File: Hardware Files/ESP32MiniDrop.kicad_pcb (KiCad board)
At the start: 2 copper layers, 74 x 54 mm, 52 parts, among them J1 USB_B_Mini, J2 Barrel_Jack, J3 AudioJack3, J4 Solenoid1 Terminal, J5 0.100" 2x4 Header, Q1 S8050, Q2 S8050, Q3 NMOS 60V 46A, SW1 SPST (RED), SW2 SPST (BLUE)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

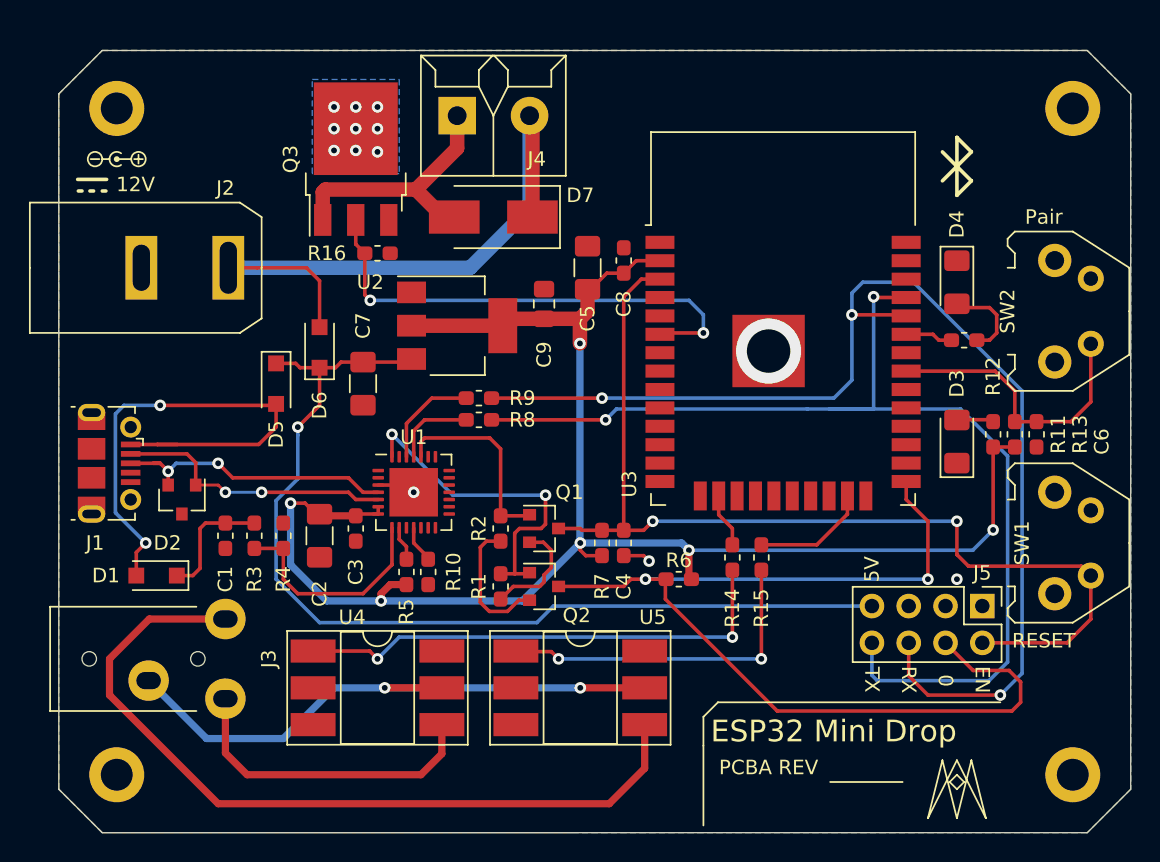
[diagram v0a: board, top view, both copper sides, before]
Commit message: Update project footprint library
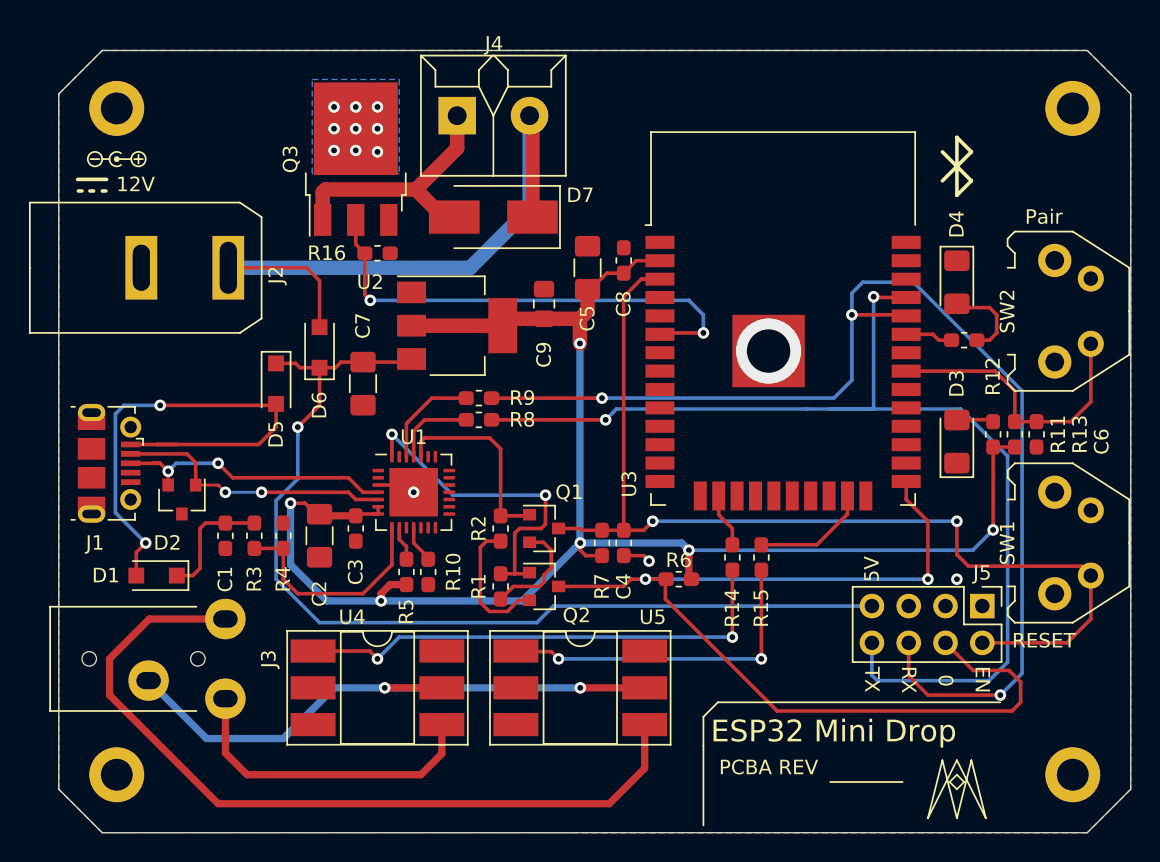
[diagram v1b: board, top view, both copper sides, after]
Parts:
- J2: footprint ESP32 Drop Controller:PJ-037A -> ESP32MiniDrop_PCB_Library:PJ-037A
- J3: footprint ESP32 Drop Controller:STX-3000 -> ESP32MiniDrop_PCB_Library:STX-3000
- J4: footprint ESP32 Drop Controller:1935161 -> ESP32MiniDrop_PCB_Library:1935161
- R1, R10, R13, R16, R2, R6, R7: value 10k -> 10k 1% 0.1W
- SW1, SW2: footprint ESP32 Drop Controller:1825027-8 -> ESP32MiniDrop_PCB_Library:1825027-8

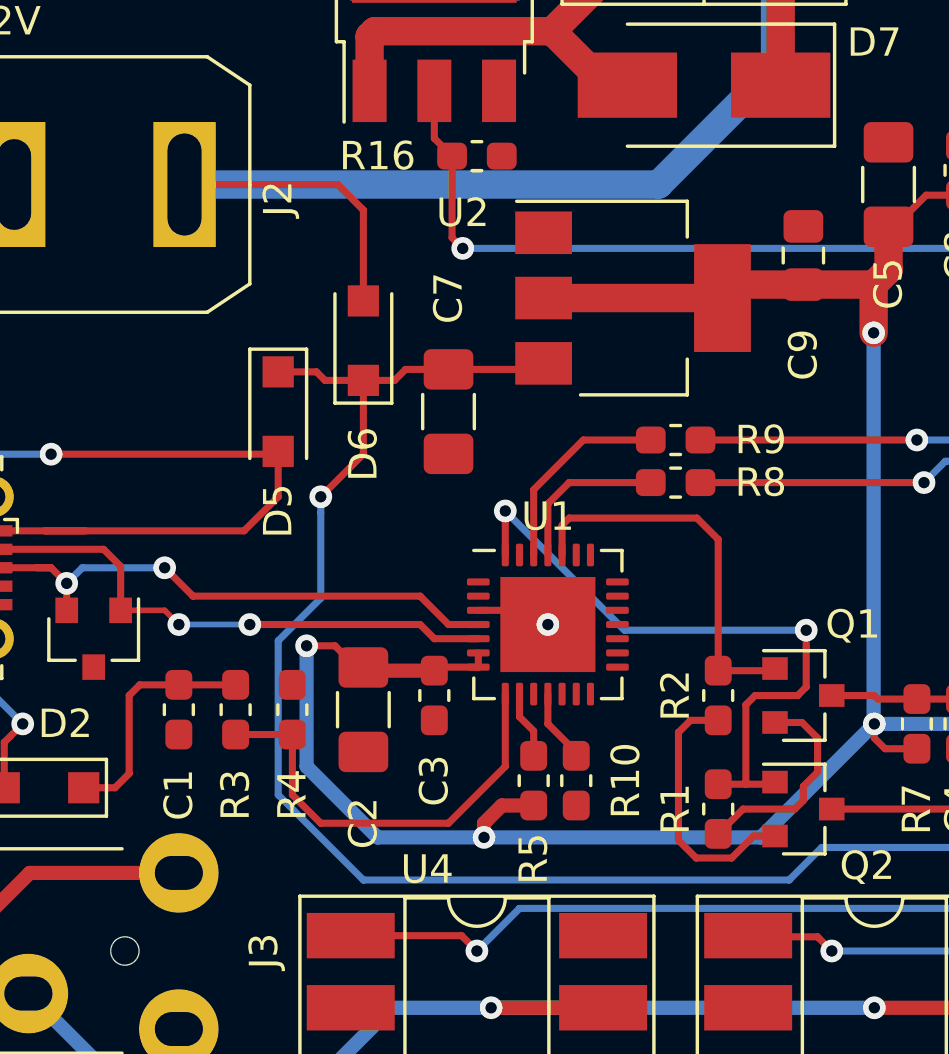
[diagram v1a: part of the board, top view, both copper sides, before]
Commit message: Add polygon pour to VREG IN
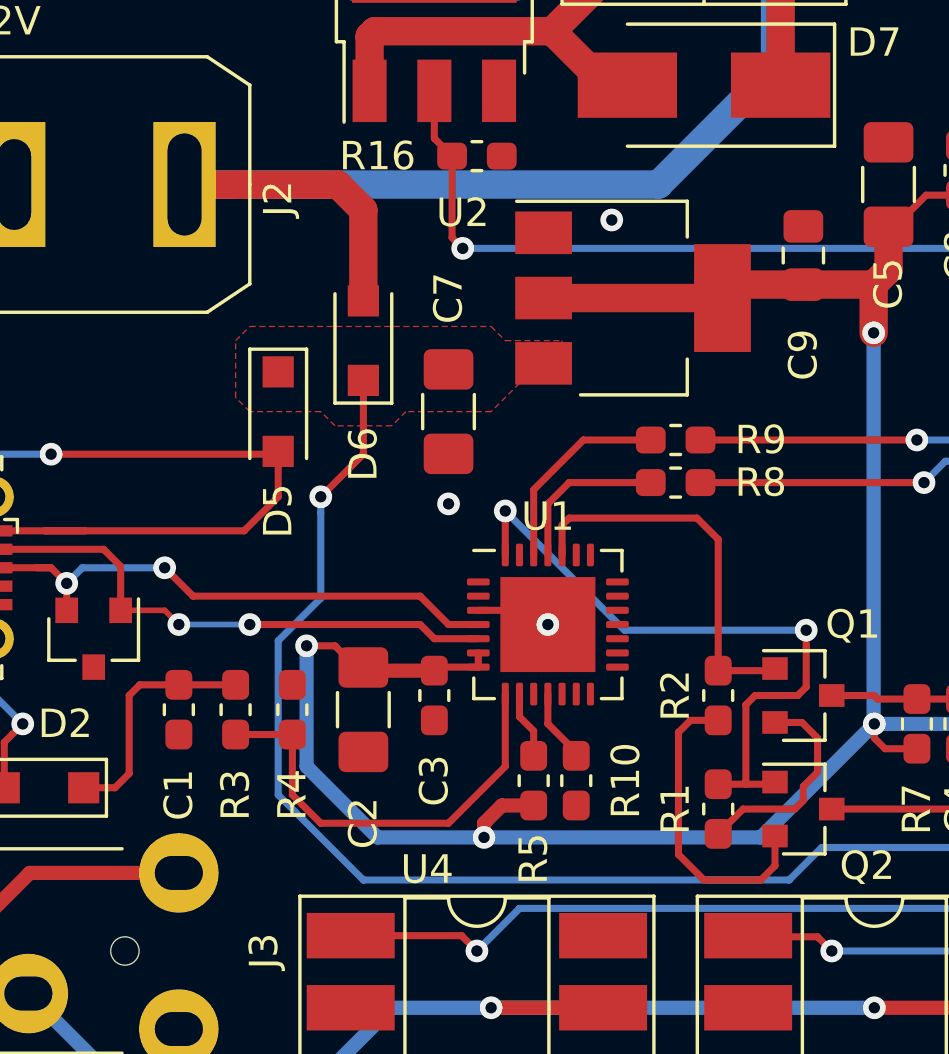
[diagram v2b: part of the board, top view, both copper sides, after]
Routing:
- net /VREG_IN: track 68.5 -> 59.1 mm
- net Net-(Q2-Pad2): track 9.36 -> 10.9 mm
- net GND: vias 4 -> 6
- added copper zone on F.Cu, net /VREG_IN

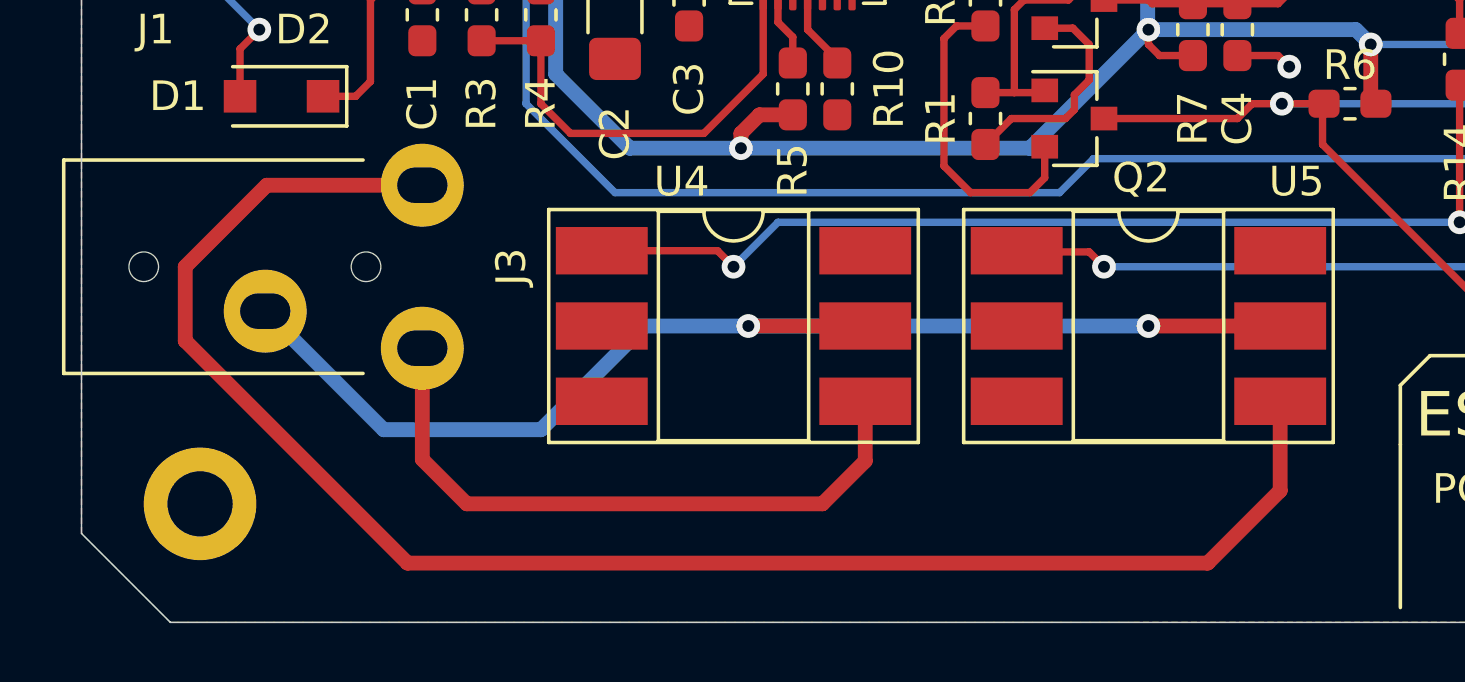
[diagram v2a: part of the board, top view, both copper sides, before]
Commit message: fix shutter control hookup
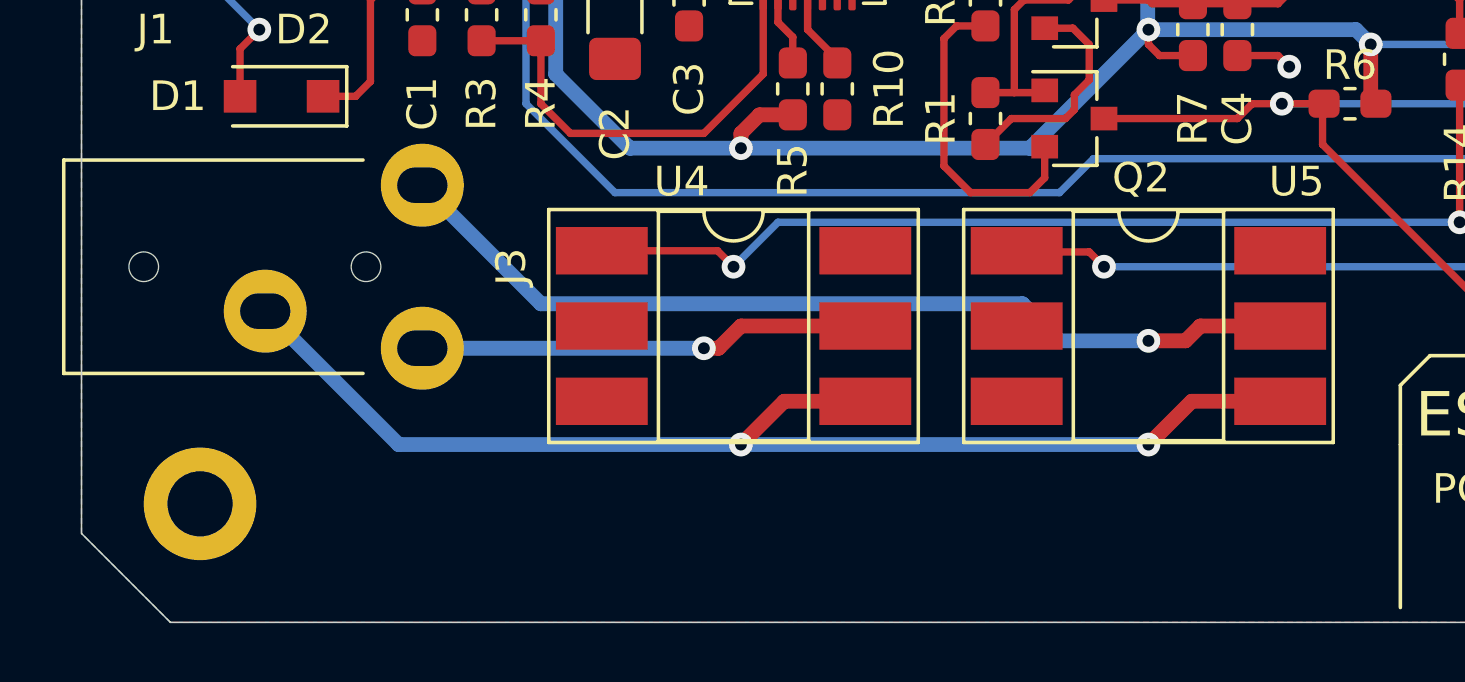
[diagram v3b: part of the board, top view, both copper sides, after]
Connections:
- U4 pad 4: Net-(J3-PadR) -> Net-(J3-PadS)
- U4 pad 5: Net-(J3-PadS) -> Net-(J3-PadR)
- U5 pad 4: Net-(J3-PadT) -> Net-(J3-PadS)
- U5 pad 5: Net-(J3-PadS) -> Net-(J3-PadT)
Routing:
- net Net-(J3-PadT): track 55.7 -> 31.3 mm, vias 0 -> 1
- net Net-(J3-PadR): track 21.9 -> 15.3 mm, vias 0 -> 1

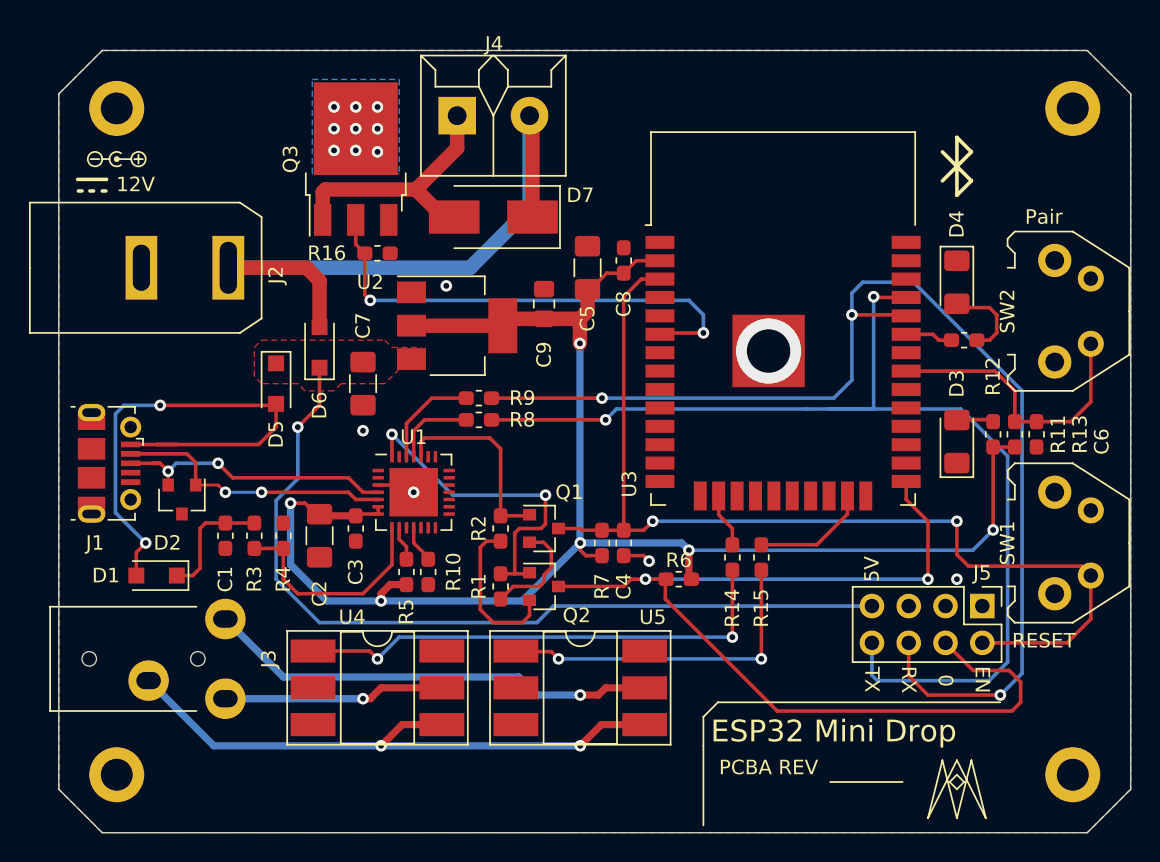
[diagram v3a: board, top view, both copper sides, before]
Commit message: Fix pin mapping error on Q1, Q2
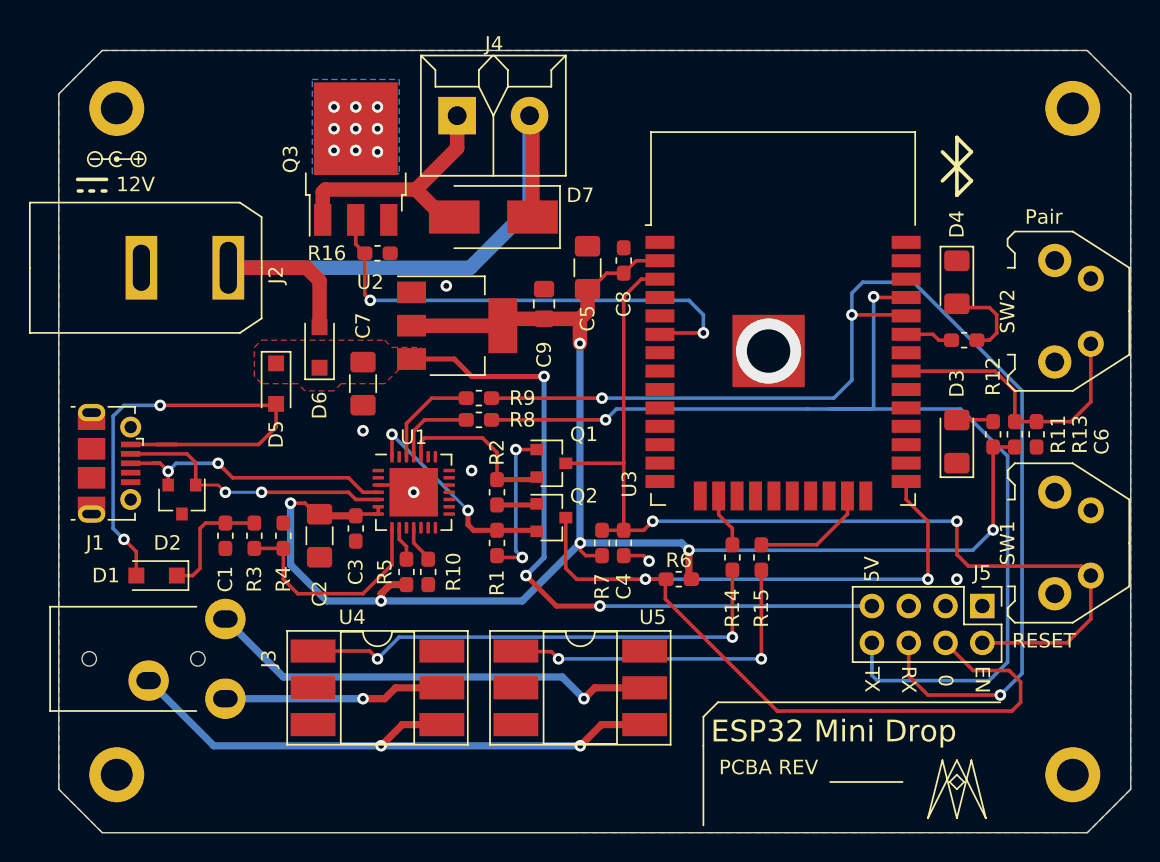
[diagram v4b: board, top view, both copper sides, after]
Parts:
- moved Q2 4.78 mm to (34.0, 32.2)
- moved Q1 4.53 mm to (34.0, 28.5)
- moved R1 3.01 mm to (30.2, 34.0)
- moved R2 2.51 mm to (30.2, 30.5)
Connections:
- Q1 pad 1: /RTS -> Net-(Q1-Pad1)
- Q1 pad 2: Net-(Q1-Pad2) -> /RTS
- Q2 pad 1: /DTR -> Net-(Q2-Pad1)
- Q2 pad 2: Net-(Q2-Pad2) -> /DTR
- R1 pad 1: Net-(Q1-Pad2) -> Net-(Q1-Pad1)
- R2 pad 1: Net-(Q2-Pad2) -> Net-(Q2-Pad1)
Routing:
- net Net-(Q2-Pad2): track 10.9 -> 0.00 mm
- net Net-(Q1-Pad1): track 0.00 -> 10.9 mm, vias 0 -> 2
- net /VREG_IN: track 59.1 -> 49.1 mm, vias 1 -> 3
- net /DTR: track 23.1 -> 14.9 mm
- net Net-(Q1-Pad2): track 7.62 -> 0.00 mm
- net /IO0: track 71.6 -> 74.7 mm
- net Net-(Q2-Pad1): track 0.00 -> 2.78 mm
- net /RTS: track 13.6 -> 11.5 mm
- net /EN: track 70.3 -> 71.2 mm
- net GND: vias 6 -> 7

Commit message: Fix transistor Q3 gate connection
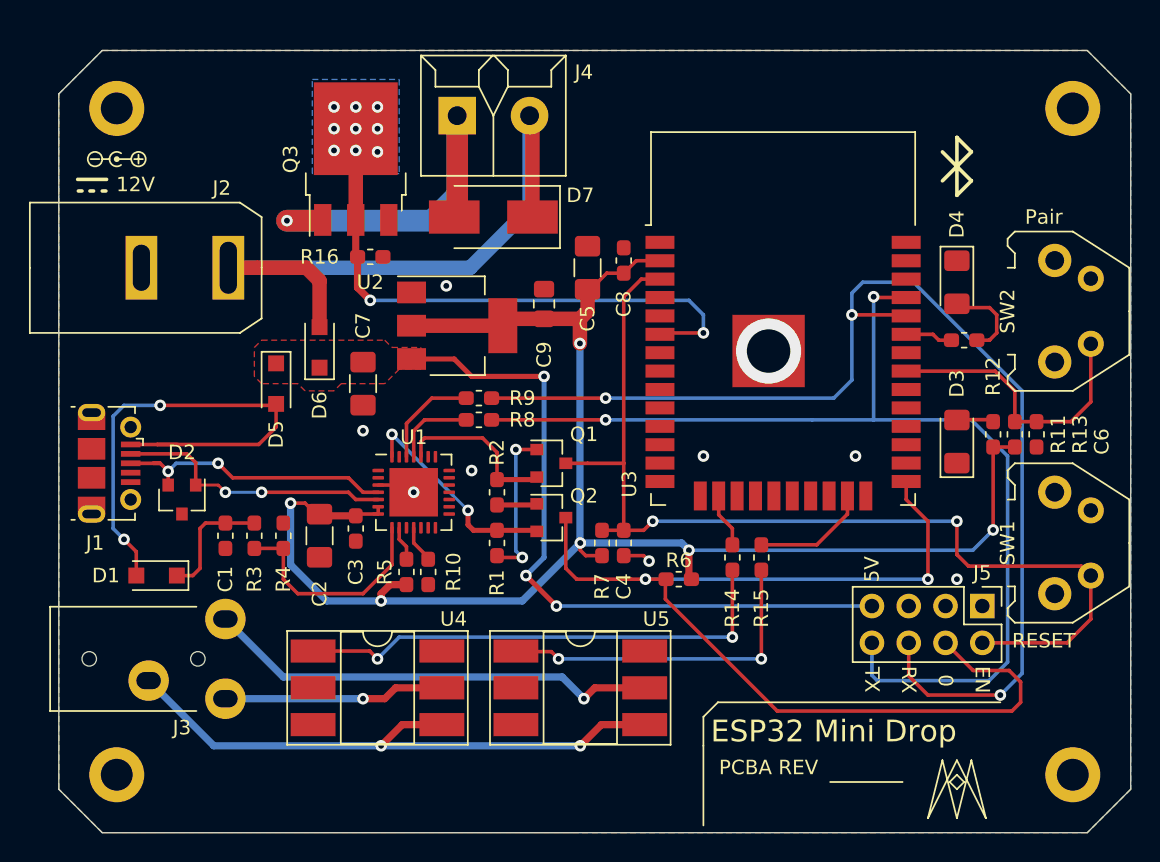
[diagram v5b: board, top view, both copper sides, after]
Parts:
- moved R16 0.56 mm to (21.5, 14.2)
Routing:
- net Net-(D7-Pad2): track 18.7 -> 28.1 mm, vias 0 -> 1
- net Solenoid_1_CTLO: track 33.7 -> 38.5 mm
- net /USB_RX: track 76.9 -> 73.9 mm
- net GND: vias 7 -> 9
